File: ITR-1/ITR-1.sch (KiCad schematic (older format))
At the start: 49 parts, among them K1 Кнопка_KLS7-TS5401-1.35-250-T, K2 Кнопка_KLS7-TS5401-1.35-250-T, K3 кнопка, K4 кнопка, X1 отверстие_под_пайку, X2 отверстие_под_пайку, X3 отверстие_под_пайку, X4 отверстие_под_пайку

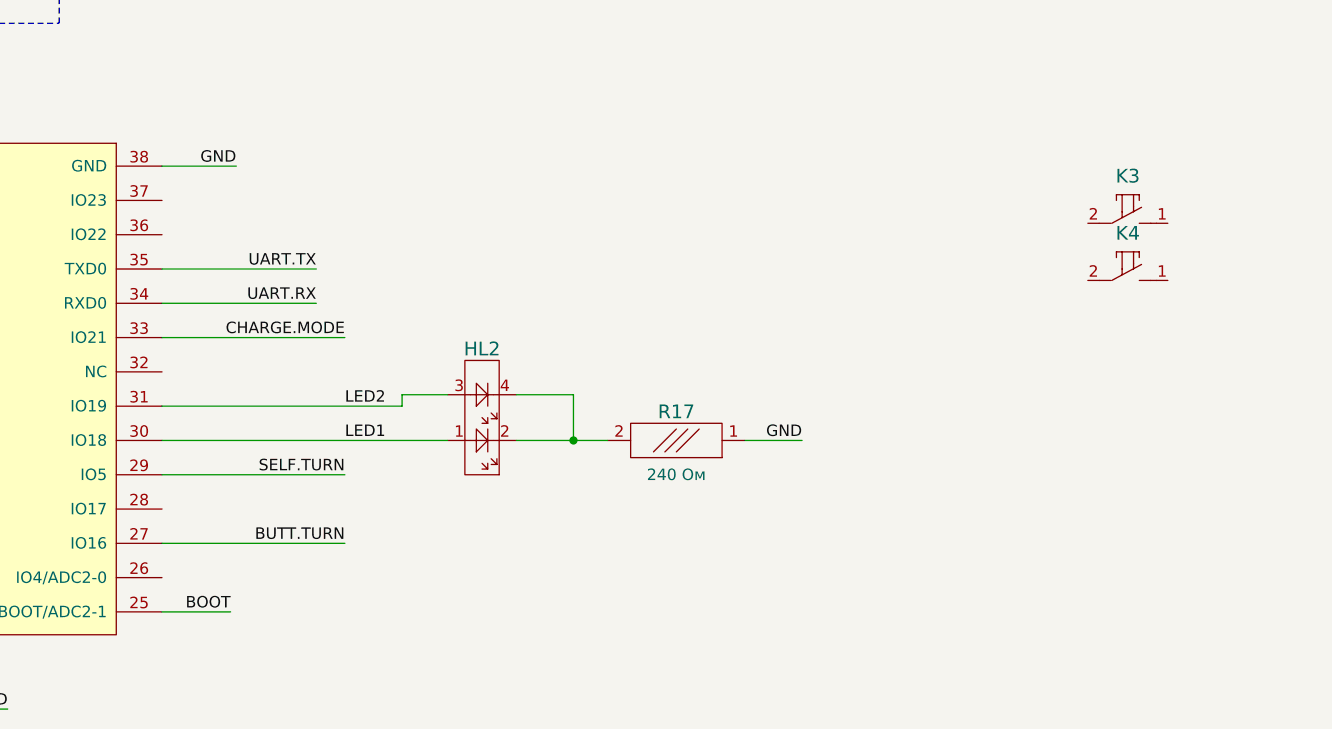
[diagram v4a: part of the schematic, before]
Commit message: ITR-1-1NN(45x30): +2 отв. под внеш. кнопки, -избыт. защита входов
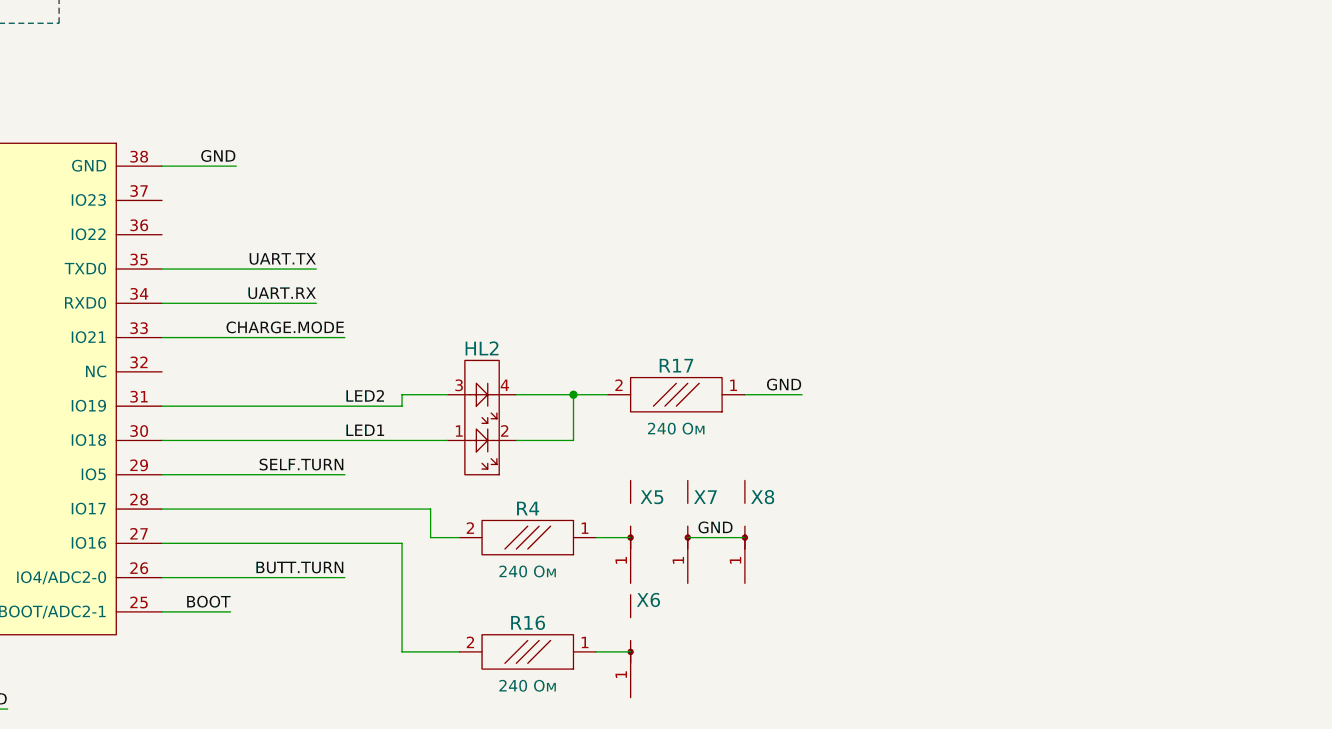
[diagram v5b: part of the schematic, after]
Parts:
- removed K3, K4: кнопка, N_X:Кнопка_FSMSM, symbol elements:кнопка
- added R16, R4: Резистор_0,065Вт, N_RLC:Резистор_SMD_0603_0,065_Вт, symbol elements:Резистор_0,065Вт
- added X5, X6, X7, X8: отверстие_под_пайку, N_X:ОтверстиеD1.2, symbol elements:отверстие_под_пайку
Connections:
- net BUTT.TURN: now also A1.26 (IO4/ADC2-0); no longer A1.27 (IO16)
- net GND: now also X7.1, X8.1
- net at A1.28 (IO17): now also R4.2
- new net: A1.27 (IO16), R16.2
- new net: R16.1, X6.1
- new net: R4.1, X5.1
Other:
- moved on the sheet: R17
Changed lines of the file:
@@
 Text Label 6750 9250 2    50   ~ 0
 CHARGE.MODE
-Text Label 6750 10150 2    50   ~ 0
+Text Label 6750 10300 2    50   ~ 0
 BUTT.TURN
 Text Label 2125 8800 0    50   ~ 0
@@
 L elements:Резистор_0,065Вт R17
 U 1 1 61468C4F
-P 8200 9700
-F 0 "R17" H 8200 9575 60  0000 C CNN
-F 1 "Резистор_0,065Вт" H 8200 9550 60  0001 C CNN
-F 2 "N_RLC:Резистор_SMD_0603_0,065_Вт" H 8200 9700 60  0001 C CNN
-F 3 "" H 8200 9700 60  0001 C CNN
-F 4 "R101" H 8200 9700 50  0001 C CNN "УГО"
-F 5 "240 Ом" H 8200 9850 50  0000 C CNN "INFO"
-	1    8200 9700
+P 8200 9500
+F 0 "R17" H 8200 9375 60  0000 C CNN
+F 1 "Резистор_0,065Вт" H 8200 9350 60  0001 C CNN
+F 2 "N_RLC:Резистор_SMD_0603_0,065_Вт" H 8200 9500 60  0001 C CNN
+F 3 "" H 8200 9500 60  0001 C CNN
+F 4 "R101" H 8200 9500 50  0001 C CNN "УГО"
+F 5 "240 Ом" H 8200 9650 50  0000 C CNN "INFO"
+	1    8200 9500
 	-1   0    0    1
 $EndComp
@@
 	1750 9400 2500 9400
 Wire Wire Line
-	5950 10150 6750 10150
-Text Label 8750 9700 2    50   ~ 0
+	5950 10300 6750 10300
+Text Label 8750 9500 2    50   ~ 0
 GND
 Wire Wire Line
@@
 	7750 9500 7500 9500
 Wire Wire Line
-	7900 9700 7750 9700
-Connection ~ 7750 9700
-Wire Wire Line
-	8750 9700 8500 9700
+	7900 9500 7750 9500
+Wire Wire Line
+	8750 9500 8500 9500
 $Comp
 L elements_2020:UBS-type-C-105450-0101&упрощенная XS3
@@
 Wire Wire Line
 	-2500 8300 -2500 8000
-$Comp
-L elements:кнопка K3
-U 1 1 61B34F09
-P 10350 8750
-F 0 "K3" H 10175 8956 60  0000 C CNN
-F 1 "кнопка" H 10175 8956 60  0001 C CNN
-F 2 "N_X:Кнопка_FSMSM" H 10225 8800 60  0001 C CNN
-F 3 "" H 10225 8800 60  0001 C CNN
-	1    10350 8750
-	1    0    0    -1
-$EndComp
 Wire Wire Line
 	7400 4250 9375 4250
@@
 	3350 6000 3875 6000
 $Comp
-L elements:кнопка K4
-U 1 1 61C0E62A
-P 10350 9000
-F 0 "K4" H 10175 9206 60  0000 C CNN
-F 1 "кнопка" H 10175 9206 60  0001 C CNN
-F 2 "N_X:Кнопка_FSMSM" H 10225 9050 60  0001 C CNN
-F 3 "" H 10225 9050 60  0001 C CNN
-	1    10350 9000
-	1    0    0    -1
-$EndComp
+L elements:отверстие_под_пайку X6
+U 1 1 61A7B851
+P 8000 10625
+F 0 "X6" H 8025 10850 60  0000 L CNN
+F 1 "отверстие_под_пайку" H 8050 10595 60  0001 L CNN
+F 2 "N_X:ОтверстиеD1.2" H 8000 10625 60  0001 C CNN
+F 3 "" H 8000 10625 60  0001 C CNN
+	1    8000 10625
+	1    0    0    -1
+$EndComp
+$Comp
+L elements:отверстие_под_пайку X5
+U 1 1 61A7B85B
+P 8000 10125
+F 0 "X5" H 7850 10300 60  0000 L CNN
+F 1 "отверстие_под_пайку" H 8050 10095 60  0001 L CNN
+F 2 "N_X:ОтверстиеD1.2" H 8000 10125 60  0001 C CNN
+F 3 "" H 8000 10125 60  0001 C CNN
+	1    8000 10125
+	-1   0    0    -1
+$EndComp
+$Comp
+L elements:Резистор_0,065Вт R4
+U 1 1 61A9C093
+P 7550 10125
+F 0 "R4" H 7550 10000 60  0000 C CNN
+F 1 "Резистор_0,065Вт" H 7550 9975 60  0001 C CNN
+F 2 "N_RLC:Резистор_SMD_0603_0,065_Вт" H 7550 10125 60  0001 C CNN
+F 3 "" H 7550 10125 60  0001 C CNN
+F 4 "R101" H 7550 10125 50  0001 C CNN "УГО"
+F 5 "240 Ом" H 7550 10275 50  0000 C CNN "INFO"
+	1    7550 10125
+	-1   0    0    1
+$EndComp
+$Comp
+L elements:Резистор_0,065Вт R16
+U 1 1 61AA69EE
+P 7550 10625
+F 0 "R16" H 7550 10500 60  0000 C CNN
+F 1 "Резистор_0,065Вт" H 7550 10475 60  0001 C CNN
+F 2 "N_RLC:Резистор_SMD_0603_0,065_Вт" H 7550 10625 60  0001 C CNN
+F 3 "" H 7550 10625 60  0001 C CNN
+F 4 "R101" H 7550 10625 50  0001 C CNN "УГО"
+F 5 "240 Ом" H 7550 10775 50  0000 C CNN "INFO"
+	1    7550 10625
+	-1   0    0    1
+$EndComp
+Wire Wire Line
+	7850 10125 8000 10125
+Connection ~ 7750 9500
+Wire Wire Line
+	7850 10625 8000 10625
+$Comp
+L elements:отверстие_под_пайку X7
+U 1 1 61B09806
+P 8250 10125
+F 0 "X7" H 8275 10300 60  0000 L CNN
+F 1 "отверстие_под_пайку" H 8300 10095 60  0001 L CNN
+F 2 "N_X:ОтверстиеD1.2" H 8250 10125 60  0001 C CNN
+F 3 "" H 8250 10125 60  0001 C CNN
+	1    8250 10125
+	1    0    0    -1
+$EndComp
+$Comp
+L elements:отверстие_под_пайку X8
+U 1 1 61B14BB1
+P 8500 10125
+F 0 "X8" H 8525 10300 60  0000 L CNN
+F 1 "отверстие_под_пайку" H 8550 10095 60  0001 L CNN
+F 2 "N_X:ОтверстиеD1.2" H 8500 10125 60  0001 C CNN
+F 3 "" H 8500 10125 60  0001 C CNN
+	1    8500 10125
+	1    0    0    -1
+$EndComp
+Wire Wire Line
+	7000 10625 7250 10625
+Wire Wire Line
+	7125 10125 7250 10125
+Text Label 8450 10125 2    50   ~ 0
+GND
+Wire Wire Line
+	8500 10125 8250 10125
+Wire Wire Line
+	5950 10000 7125 10000
+Wire Wire Line
+	7125 10000 7125 10125
+Wire Wire Line
+	5950 10150 7000 10150
+Wire Wire Line
+	7000 10150 7000 10625
 $EndSCHEMATC
